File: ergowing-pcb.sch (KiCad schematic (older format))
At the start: 16 parts, among them J1 USB_mini_micro_B, SW1 SW_PUSH, U1 ATMEGA32U4, X1 XTAL_GND

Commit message: Revert "Rows re-wired to be cleaner"
This reverts commit 00a00da537b04bf894fe4a5768944e963a032eb3.
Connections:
- net row0: now also U1.28 (PB4); no longer U1.31 (PC6)
- net row1: now also U1.29 (PB5); no longer U1.30 (PB6)
- net row2: now also U1.30 (PB6); no longer U1.29 (PB5)
- net row3: now also U1.31 (PC6); no longer U1.28 (PB4)
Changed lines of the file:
@@
 row4
 Text GLabel 4600 3950 2    60   Input ~ 0
+row3
+Text GLabel 4600 4050 2    60   Input ~ 0
+row2
+Text GLabel 4600 4150 2    60   Input ~ 0
+row1
+Text GLabel 4600 4250 2    60   Input ~ 0
 row0
-Text GLabel 4600 4050 2    60   Input ~ 0
-row1
-Text GLabel 4600 4150 2    60   Input ~ 0
-row2
-Text GLabel 4600 4250 2    60   Input ~ 0
-row3
 Text GLabel 2450 3650 0    60   Input ~ 0
 col0

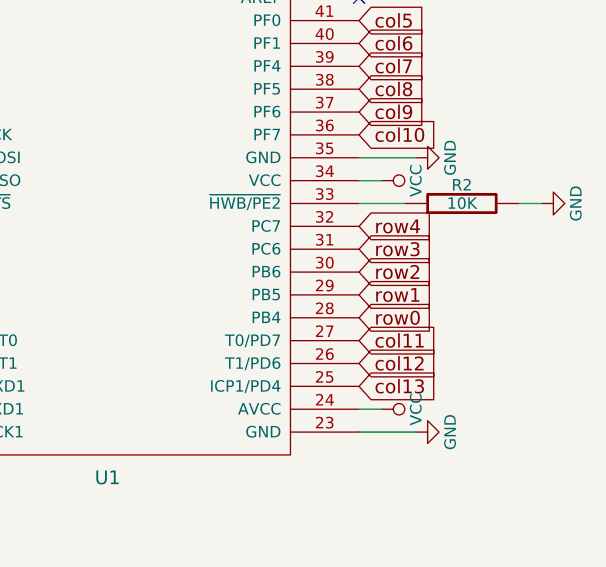
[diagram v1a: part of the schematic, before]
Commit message: Rows re-wired to be cleaner
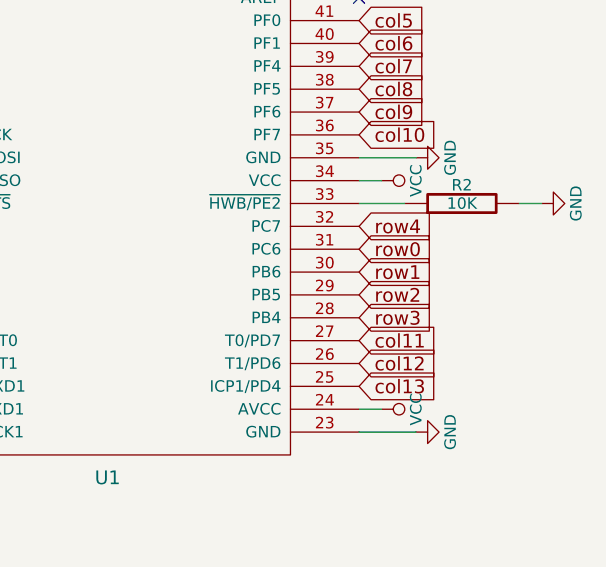
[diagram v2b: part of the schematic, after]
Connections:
- net row0: now also U1.31 (PC6); no longer U1.28 (PB4)
- net row1: now also U1.30 (PB6); no longer U1.29 (PB5)
- net row2: now also U1.29 (PB5); no longer U1.30 (PB6)
- net row3: now also U1.28 (PB4); no longer U1.31 (PC6)
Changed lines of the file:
@@
 row4
 Text GLabel 4600 3950 2    60   Input ~ 0
+row0
+Text GLabel 4600 4050 2    60   Input ~ 0
+row1
+Text GLabel 4600 4150 2    60   Input ~ 0
+row2
+Text GLabel 4600 4250 2    60   Input ~ 0
 row3
-Text GLabel 4600 4050 2    60   Input ~ 0
-row2
-Text GLabel 4600 4150 2    60   Input ~ 0
-row1
-Text GLabel 4600 4250 2    60   Input ~ 0
-row0
 Text GLabel 2450 3650 0    60   Input ~ 0
 col0

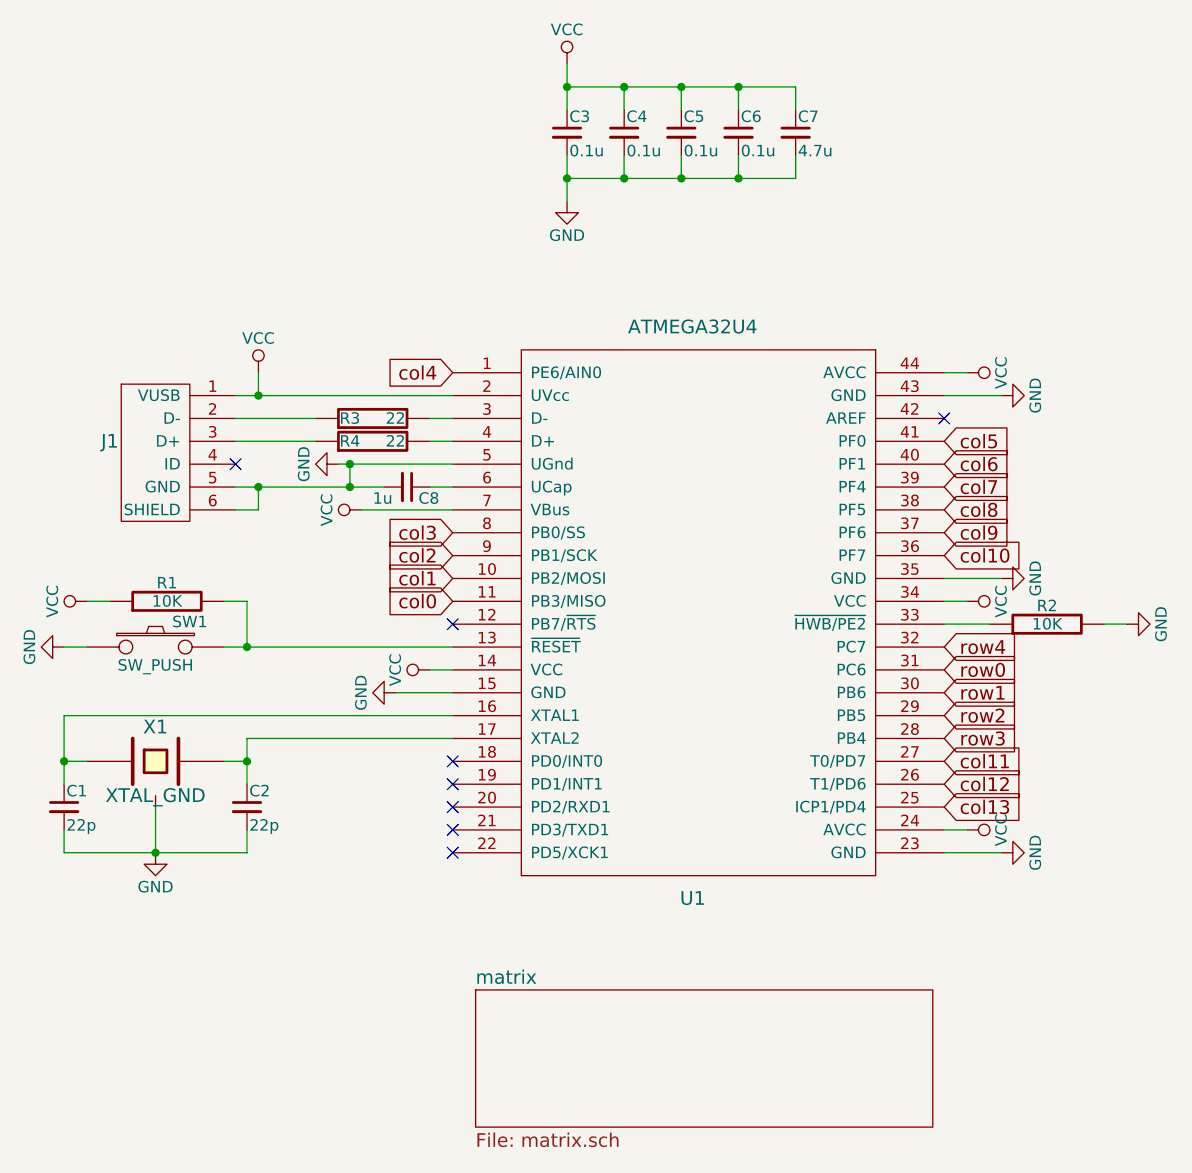
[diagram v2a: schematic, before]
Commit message: Re-wire C5, C7, C8. Adjust row3
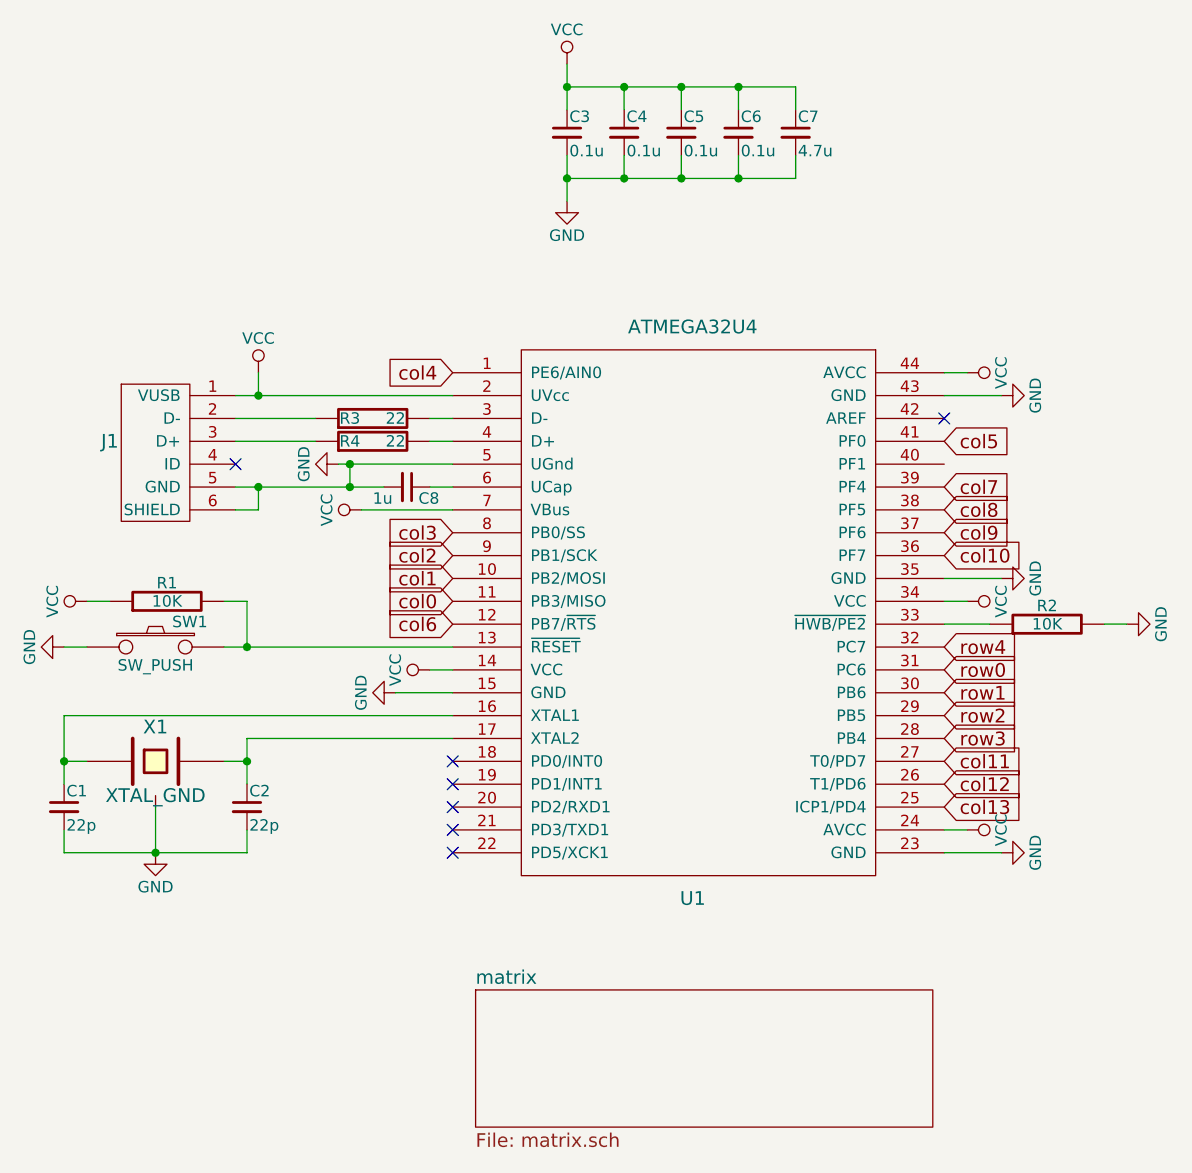
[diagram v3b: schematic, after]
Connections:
- net col6: now also U1.12 (PB7/~RTS); no longer U1.40 (PF1)
- no-connect marks 8 -> 7
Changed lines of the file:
@@
 	1150 4550 1150 4750
 Wire Wire Line
-	2950 1900 2950 1700
+	2950 1700 2950 1900
 Wire Wire Line
-	2950 1500 2950 1300
+	2950 1300 2950 1500
 Wire Wire Line
 	2950 1400 3950 1400
@@
 	2450 3150 2350 3150
 Wire Wire Line
-	2150 3150 1500 3150
+	1500 3150 2150 3150
 Wire Wire Line
 	2000 3050 2000 3150
@@
 Text GLabel 4600 2950 2    60   Input ~ 0
 col5
-Text GLabel 4600 3050 2    60   Input ~ 0
+Text GLabel 2450 3750 0    60   Input ~ 0
 col6
 Text GLabel 4600 3150 2    60   Input ~ 0
@@
 	0    -1   -1   0
 $EndComp
-NoConn ~ 2450 3750
 NoConn ~ 2450 4350
 NoConn ~ 2450 4450

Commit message: Cols done
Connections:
- net row0 is gone; now on net col3: U1.31 (PC6)
- net col0: now also U1.28 (PB4); no longer U1.11 (PB3/MISO)
- net col1: now also U1.29 (PB5); no longer U1.10 (PB2/MOSI)
- net col10: now also U1.32 (PC7); no longer U1.36 (PF7)
- net col2: now also U1.30 (PB6); no longer U1.9 (PB1/SCK)
- net col3: no longer U1.8 (PB0/SS)
- net row1: now also U1.11 (PB3/MISO); no longer U1.30 (PB6)
- net row2: now also U1.10 (PB2/MOSI); no longer U1.29 (PB5)
- net row3: now also U1.9 (PB1/SCK); no longer U1.28 (PB4)
- net row4: now also U1.36 (PF7), U1.8 (PB0/SS); no longer U1.32 (PC7)
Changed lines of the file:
@@
 	4600 4750 4850 4750
 Text GLabel 4600 3850 2    60   Input ~ 0
+col10
+Text GLabel 4600 3950 2    60   Input ~ 0
+col3
+Text GLabel 4600 4050 2    60   Input ~ 0
+col2
+Text GLabel 4600 4150 2    60   Input ~ 0
+col1
+Text GLabel 4600 4250 2    60   Input ~ 0
+col0
+Text GLabel 2450 3650 0    60   Input ~ 0
+row1
+Text GLabel 2450 3550 0    60   Input ~ 0
+row2
+Text GLabel 2450 3450 0    60   Input ~ 0
+row3
+Text GLabel 2450 3350 0    60   Input ~ 0
 row4
-Text GLabel 4600 3950 2    60   Input ~ 0
-row0
-Text GLabel 4600 4050 2    60   Input ~ 0
-row1
-Text GLabel 4600 4150 2    60   Input ~ 0
-row2
-Text GLabel 4600 4250 2    60   Input ~ 0
-row3
-Text GLabel 2450 3650 0    60   Input ~ 0
-col0
-Text GLabel 2450 3550 0    60   Input ~ 0
-col1
-Text GLabel 2450 3450 0    60   Input ~ 0
-col2
-Text GLabel 2450 3350 0    60   Input ~ 0
-col3
 Text GLabel 2450 2650 0    60   Input ~ 0
 col4
@@
 col9
 Text GLabel 4600 3450 2    60   Input ~ 0
-col10
+row4
 Text GLabel 4600 4350 2    60   Input ~ 0
 col11
